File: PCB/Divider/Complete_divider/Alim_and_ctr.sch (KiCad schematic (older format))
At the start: 43 parts

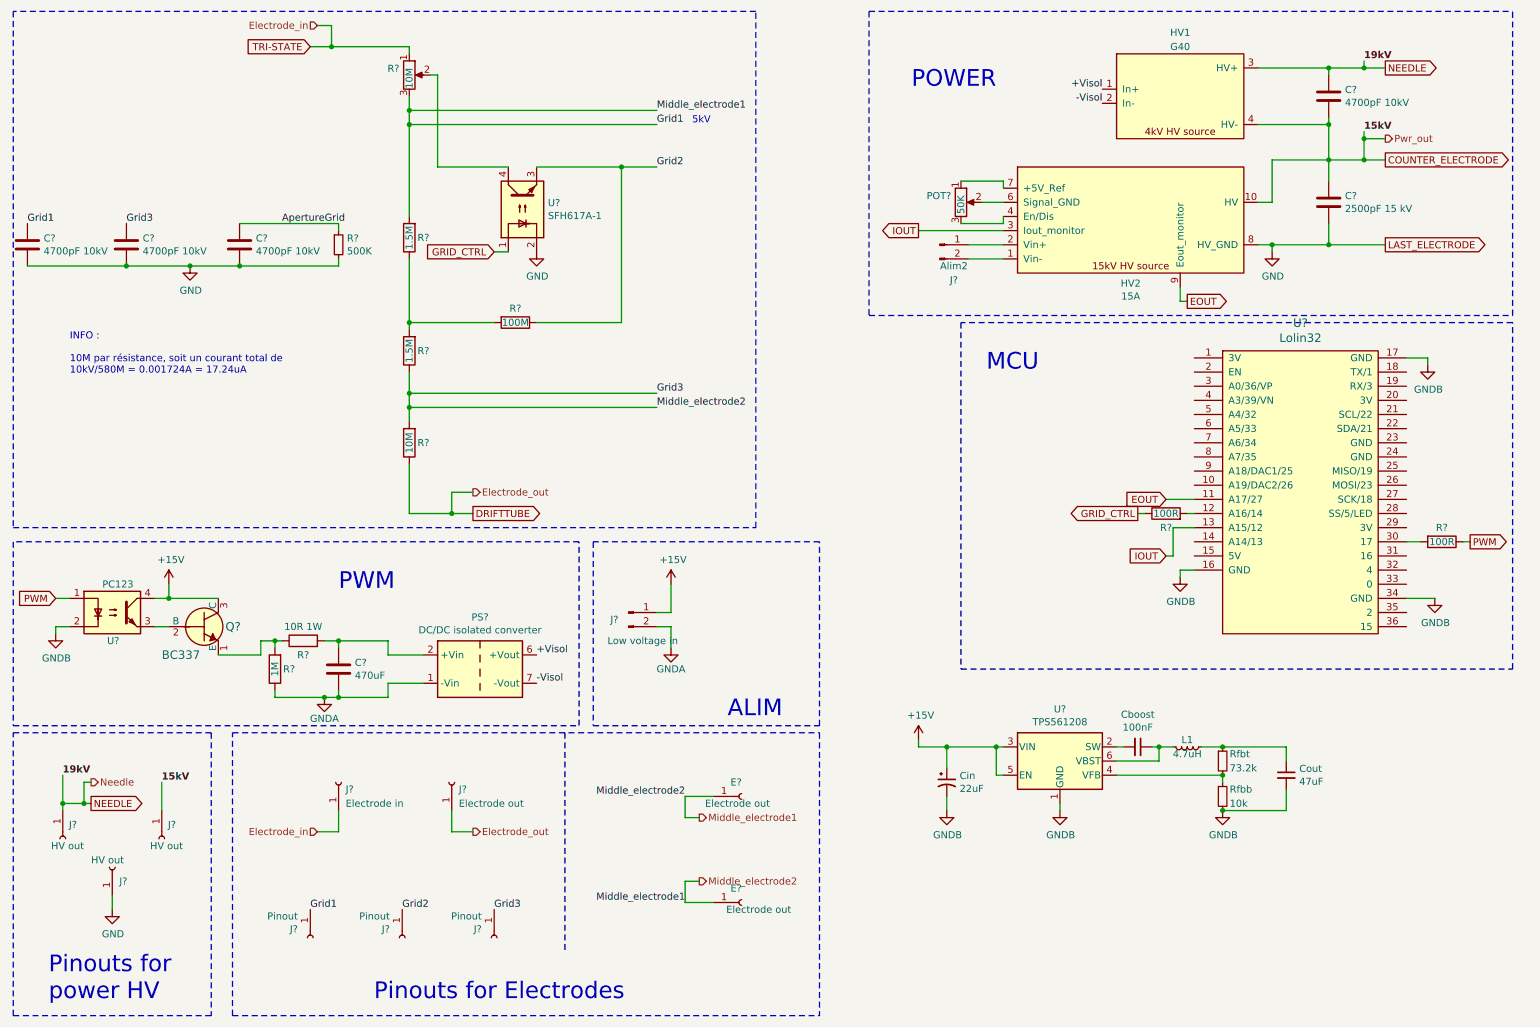
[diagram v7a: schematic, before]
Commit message: DC/DC isolated converter implementation
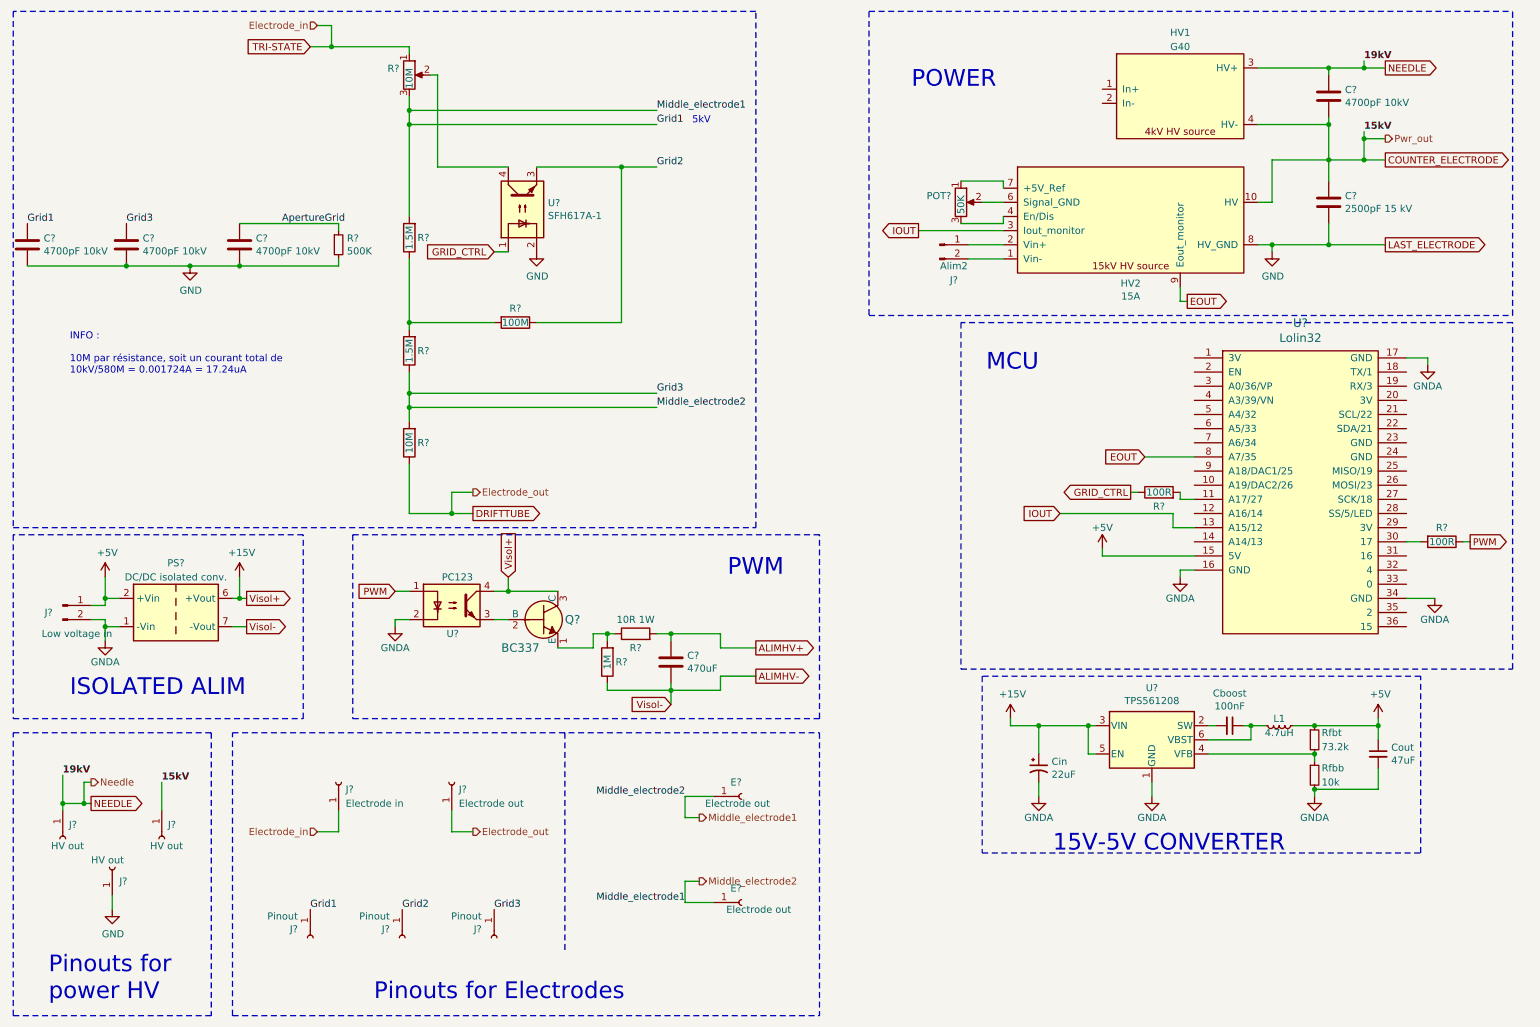
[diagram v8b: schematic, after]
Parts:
- PS?: value DC/DC isolated converter -> DC/DC isolated conv.
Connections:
- net +15V: now also PS?.6 (+Vout); no longer J?.1 (Pin_1)
- net EOUT: now also U?.8 (A7/35); no longer U?.11 (A17/27)
- net GNDA: no longer C?.2, R?.1
- net at R?.2: now also U?.11 (A17/27); no longer U?.12 (A16/14)
- net ALIMHV+: now reaches C?.1, R?.2
- net ALIMHV+: no longer PS?.2 (+Vin)
- net +5V: now reaches U?.15 (5V)
- net +5V: now also Cout.1, J?.1 (Pin_1), L1.1, PS?.2 (+Vin), Rfbt.1
- net +Visol: no longer names the net of HV1.1 (In+)
- net +Visol: no longer PS?.6 (+Vout)
- net -Visol: no longer names the net of HV1.2 (In-)
- net -Visol: no longer PS?.7 (-Vout)
- new net ALIMHV-: C?.2, PS?.7 (-Vout), R?.1
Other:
- note added: "15V-5V CONVERTER\n"
- note added: "ISOLATED ALIM\n"
- note removed: "ALIM\n"
- moved on the sheet: C?, Cboost, Cin, Cout, J?, L1, PS?, Q?, R?, Rfbb, Rfbt, U?
